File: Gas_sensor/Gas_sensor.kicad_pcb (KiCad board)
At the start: 2 copper layers, 100 x 73.5 mm, 69 parts, among them J1 Fix, J2 Fix, J3 Conn_01x03, J4 Conn_01x03, J5 Conn_01x03, J6 Conn_01x03, P1 Prog, Q1 PMV65UN, SW1 SW_Push, SW2 SW_Push, SW3 SW_Push, SW4 SW_Power, U1 MAX7219, U10 TPS61032PWP, U2 SCA103T-D04, U3 7SEGMENT_CC, U4 7SEGMENT_CC, U5 7SEGMENT_CC, U6 7SEGMENT_CC, U7 PIC16F18323_SOIC, U8 7SEGMENT_CC, U9 7SEGMENT_CC

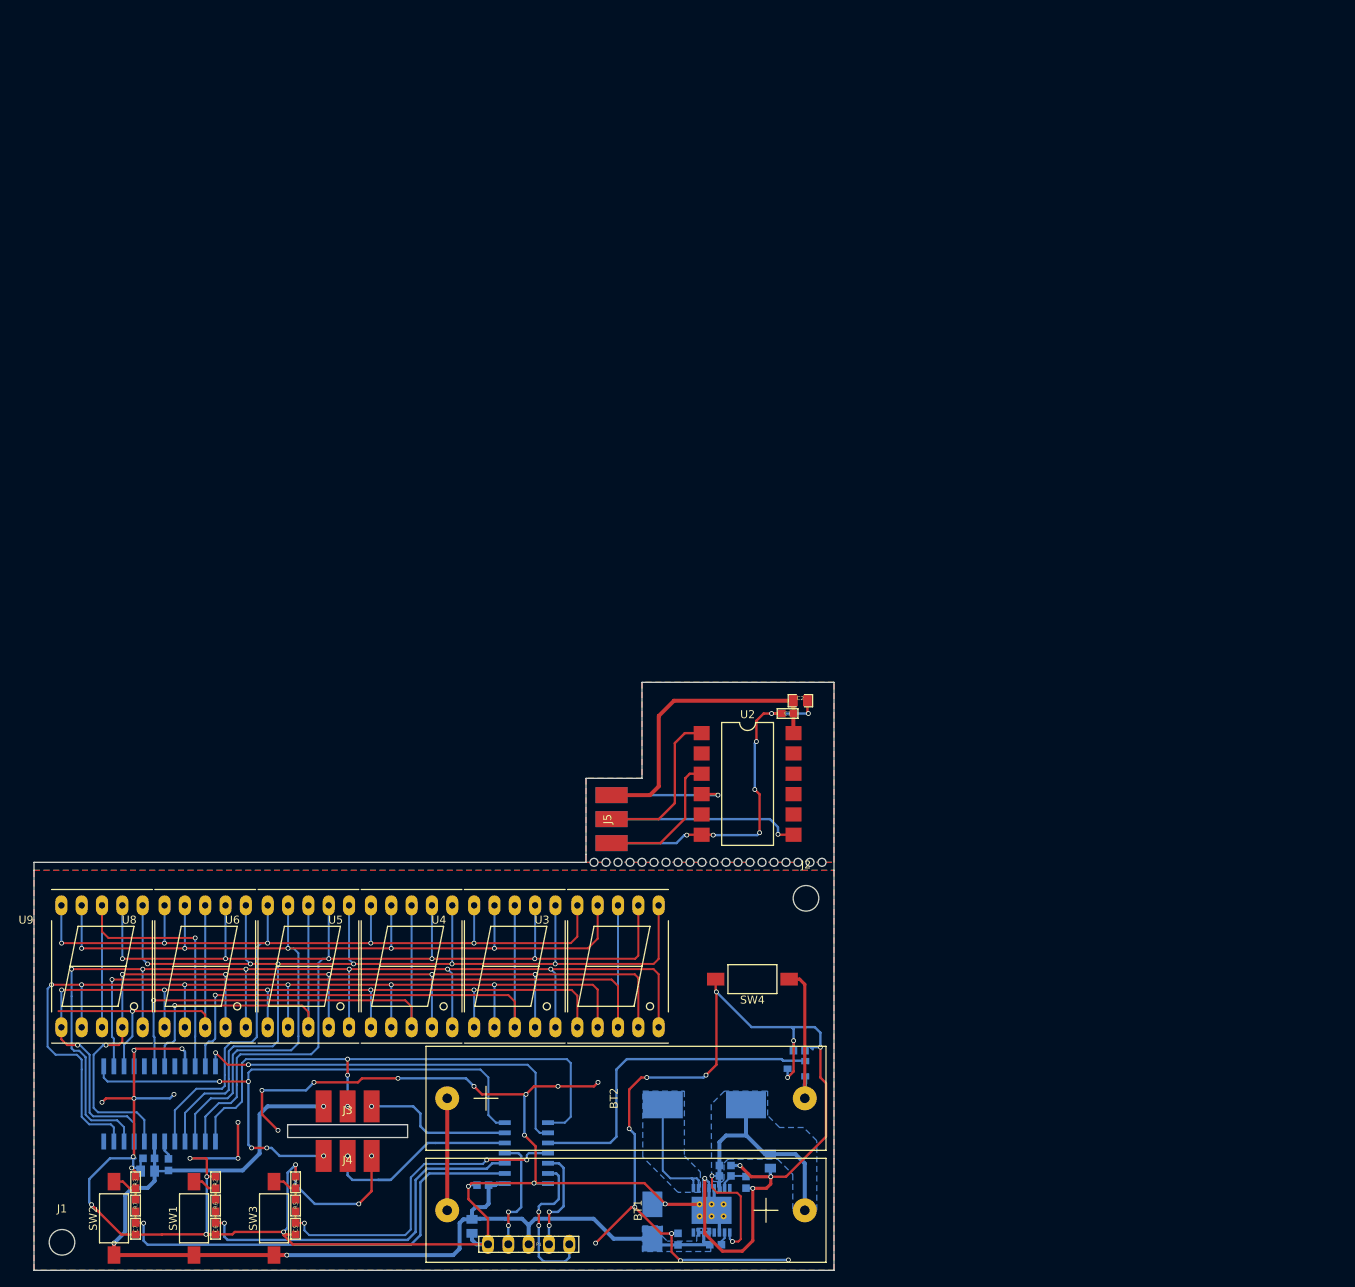
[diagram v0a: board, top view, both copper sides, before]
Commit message: update gas sensor schematic
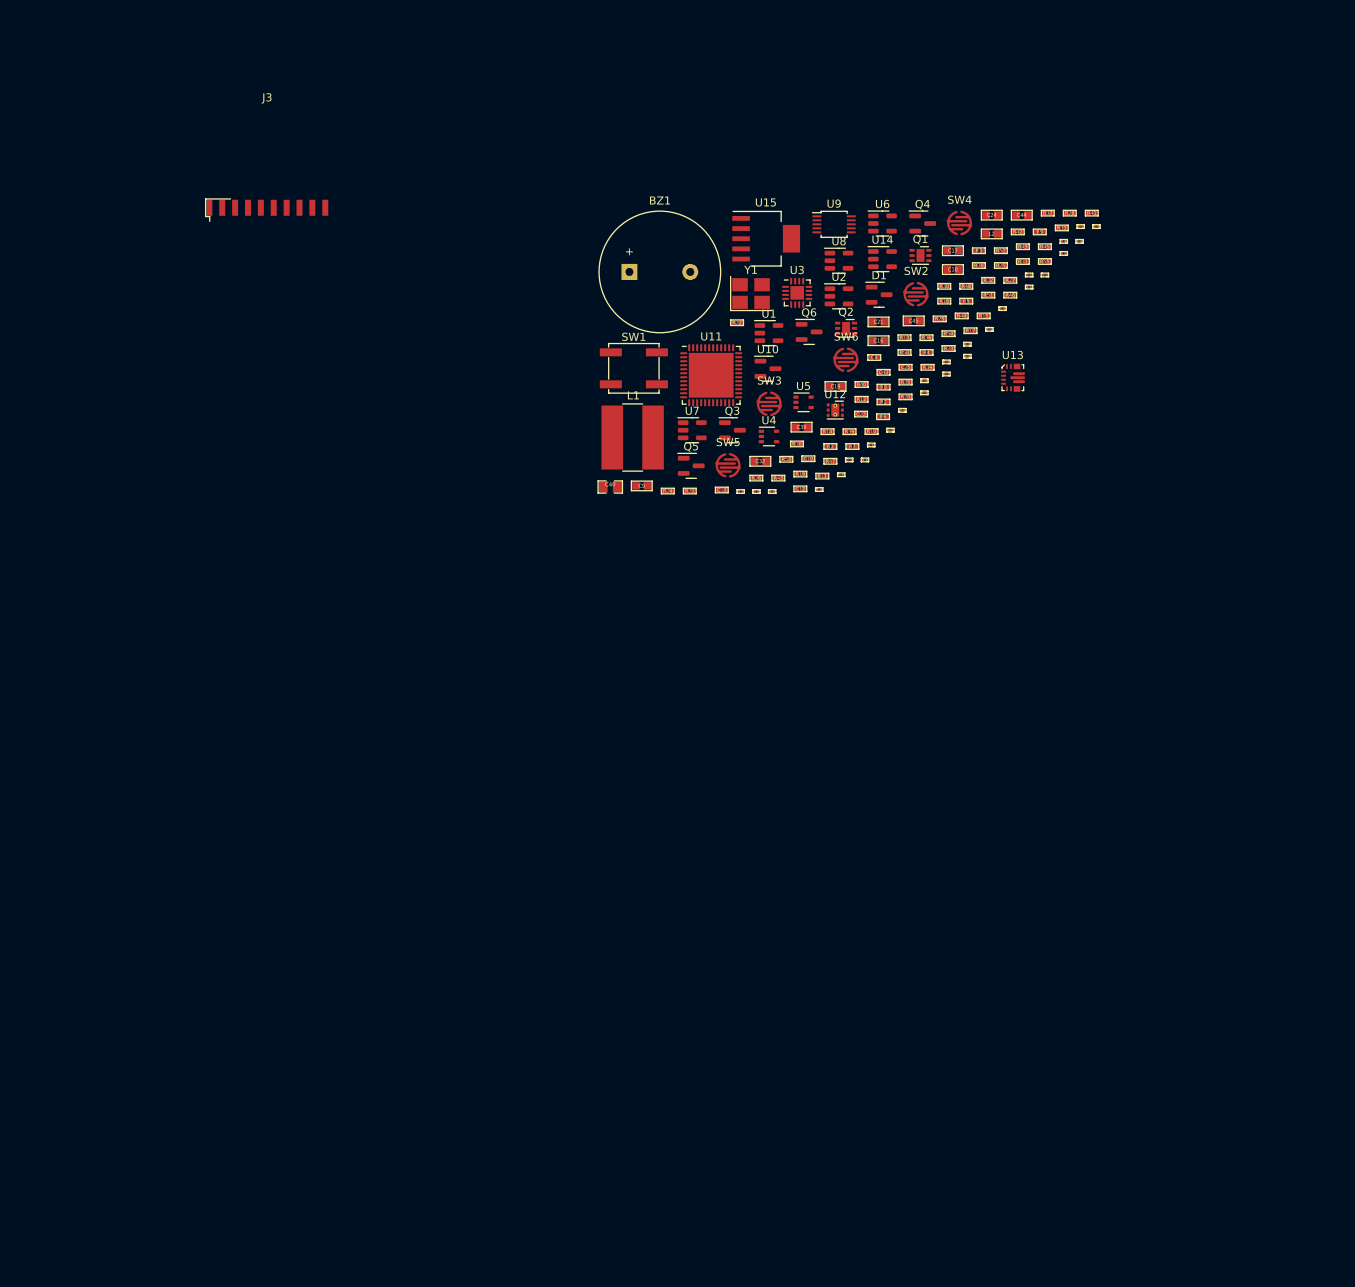
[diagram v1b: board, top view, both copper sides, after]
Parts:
- removed BT1, BT2: Keystone_2466, Yame_library:AAA_2466
- removed CutHole_1 (x20): VAL**, Yame_library:CutHole_1
- removed J1, J2: Fix, Mounting_Holes:MountingHole_3.2mm_M3
- removed J4, J5, J6: Conn_01x03, Yame_library:Inc_90°
- removed P1: Prog, Yame_library:HE10_14-5C-2.54-MR
- added BZ1: BUZZER, Buzzer_Beeper:Buzzer_15x7.5RM7.6, F.Cu at (99.4, 55.2)
- added C14: 100n, Yame_library:SM0201-MR, F.Cu at (155.7, 51.4)
- added C15: 100n, Yame_library:SM0201-MR, F.Cu at (146.1, 59.8)
- added C16: 1u, Yame_library:SM0603-MR, F.Cu at (130.6, 63.8)
- added C17: 1u, Yame_library:SM0603-MR, F.Cu at (139.9, 52.5)
- added C18: 1u, Yame_library:SM0603-MR, F.Cu at (139.9, 54.9)
- added C19: 1u, Yame_library:SM0603-MR, F.Cu at (125.2, 69.5)
- added C20: 100n, Yame_library:SM0201-MR, F.Cu at (133.6, 72.5)
- added C21: 2.2u, Yame_library:SM0603-MR, F.Cu at (130.6, 61.5)
- added C22: 100n, Yame_library:SM0201-MR, F.Cu at (141.7, 65.7)
- added C23: 8p, Yame_library:SM0402-MR, F.Cu at (128.4, 73.0)
- added C24: 1u, Yame_library:SM0603-MR, F.Cu at (144.7, 48.1)
- added C25: 8p, Yame_library:SM0402-MR, F.Cu at (133.9, 67.1)
- added C26: 100n, Yame_library:SM0201-MR, F.Cu at (149.4, 57.1)
- added C27: 100n, Yame_library:SM0201-MR, F.Cu at (157.8, 49.5)
- added C28: 100n, Yame_library:SM0201-MR, F.Cu at (132.1, 75.0)
- added C29: 100n, Yame_library:SM0201-MR, F.Cu at (141.7, 64.2)
- added C30: 100n, Yame_library:SM0201-MR, F.Cu at (136.3, 70.3)
- added C31: 100n, Yame_library:SM0201-MR, F.Cu at (144.4, 62.4)
- added C32: 22u, Yame_library:SM0603-MR, F.Cu at (115.8, 78.9)
- added C33: 100n, Yame_library:SM0201-MR, F.Cu at (128.9, 78.7)
- added C34: 100n, Yame_library:SM0201-MR, F.Cu at (139.1, 66.5)
- added C35: 100n, Yame_library:SM0201-MR, F.Cu at (129.7, 76.8)
- added C36: 100n, Yame_library:SM0201-MR, F.Cu at (136.3, 68.8)
- added C37: 100n, Yame_library:SM0201-MR, F.Cu at (139.1, 68.0)
- added C38: 100n, Yame_library:SM0201-MR, F.Cu at (153.7, 51.4)
- added C39: 10u, Yame_library:SM0603-MR, F.Cu at (120.9, 74.6)
- added C40: 47u, Yame_library:SM0805-MR, F.Cu at (97.0, 82.1)
- added C41: 100n, Yame_library:SM0201-MR, F.Cu at (155.8, 49.5)
- added C42: 100n, Yame_library:SM0201-MR, F.Cu at (117.3, 82.7)
- added C43: 10n, Yame_library:SM0402-MR, F.Cu at (131.2, 67.8)
- added C44: 10u, Yame_library:SM0603-MR, F.Cu at (148.5, 48.1)
- added C45: 10u, Yame_library:SM0603-MR, F.Cu at (135.0, 61.3)
- added D1: BAT54C, Package_TO_SOT_SMD:SOT-23, F.Cu at (130.6, 58.0)
- added L2: L_Ferrite, Yame_library:SM0603-MR, F.Cu at (144.7, 50.5)
- added Q2: DMC1229UFDB, Package_DFN_QFN:DFN-6-1EP_2x2mm_P0.65mm_EP1x1.6mm, F.Cu at (126.5, 62.2)
- added Q3: Q_NMOS_GSD, Package_TO_SOT_SMD:SOT-23, F.Cu at (112.3, 75.0)
- added Q4: Q_NMOS_GSD, Package_TO_SOT_SMD:SOT-23, F.Cu at (136.1, 49.1)
- added Q5: Q_NMOS_GSD, Package_TO_SOT_SMD:SOT-23, F.Cu at (107.2, 79.4)
- added Q6: Q_NMOS_GSD, Package_TO_SOT_SMD:SOT-23, F.Cu at (121.9, 62.7)
- added R13: 100, Yame_library:SM0402-MR, F.Cu at (133.8, 63.4)
- added R14: 22k, Yame_library:SM0402-MR, F.Cu at (124.2, 75.2)
- added R15: 22k, Yame_library:SM0402-MR, F.Cu at (143.7, 60.7)
- added R16: 22k, Yame_library:SM0402-MR, F.Cu at (120.4, 76.7)
- added R17: 2.2k, Yame_library:SM0402-MR, F.Cu at (142.1, 62.5)
- added R18: 2.2k, Yame_library:SM0402-MR, F.Cu at (138.8, 58.9)
- added R19: 2.2k, Yame_library:SM0402-MR, F.Cu at (120.8, 80.5)
- added R20: 2.2k, Yame_library:SM0402-MR, F.Cu at (133.9, 70.8)
- added R21: 0, Yame_library:SM0402-MR, F.Cu at (107.0, 82.6)
- added R22: 0, Yame_library:SM0402-MR, F.Cu at (112.9, 61.5)
- added R23: 0, Yame_library:SM0402-MR, F.Cu at (139.3, 64.8)
- added R24: 100k, Yame_library:SM0402-MR, F.Cu at (104.2, 82.6)
- added R25: 10k, Yame_library:SM0402-MR, F.Cu at (145.9, 54.4)
- added R26: 0, Yame_library:SM0402-MR, F.Cu at (115.3, 81.0)
- added R27: 0, Yame_library:SM0402-MR, F.Cu at (147.0, 56.2)
- added R28: 0, Yame_library:SM0402-MR, F.Cu at (154.5, 47.9)
- added R29: 390k, Yame_library:SM0402-MR, F.Cu at (138.2, 61.1)
- added R30: 390k, Yame_library:SM0402-MR, F.Cu at (138.8, 57.0)
- added R31: 390k, Yame_library:SM0402-MR, F.Cu at (148.6, 53.9)
- added R32: 390k, Yame_library:SM0402-MR, F.Cu at (144.3, 56.2)
- added R33: 390k, Yame_library:SM0402-MR, F.Cu at (153.5, 49.7)
- added R34: 390k, Yame_library:SM0402-MR, F.Cu at (136.7, 67.1)
- added R35: 390k, Yame_library:SM0402-MR, F.Cu at (133.9, 69.0)
- added R36: 390k, Yame_library:SM0402-MR, F.Cu at (136.6, 63.4)
- added R37: 10k, Yame_library:SM0402-MR, F.Cu at (151.7, 47.9)
- added R38: 100k, Yame_library:SM0402-MR, F.Cu at (143.1, 54.4)
- added R39: 100k, Yame_library:SM0402-MR, F.Cu at (126.9, 75.2)
- added R40: 22k, Yame_library:SM0402-MR, F.Cu at (128.4, 69.3)
- added R41: 22k, Yame_library:SM0402-MR, F.Cu at (157.2, 47.9)
- added R42: 22k, Yame_library:SM0402-MR, F.Cu at (148.0, 50.2)
- added R43: 3.9k, Yame_library:SM0402-MR, F.Cu at (118.0, 81.0)
- added R44: 3.9k, Yame_library:SM0402-MR, F.Cu at (141.0, 60.7)
- added R45: 100k, Yame_library:SM0402-MR, F.Cu at (151.4, 52.0)
- added R46: 100k, Yame_library:SM0402-MR, F.Cu at (147.0, 58.1)
- added R47: 100k, Yame_library:SM0402-MR, F.Cu at (124.5, 78.9)
- added R48: R, Yame_library:SM0402-MR, F.Cu at (141.5, 57.0)
- added R49: 910k, Yame_library:SM0402-MR, F.Cu at (148.6, 52.0)
- added R50: 43k, Yame_library:SM0402-MR, F.Cu at (133.8, 65.3)
- added R51: 100k, Yame_library:SM0402-MR, F.Cu at (144.3, 58.1)
- added R52: 3.9k, Yame_library:SM0402-MR, F.Cu at (145.9, 52.5)
- added R53: 3.9k, Yame_library:SM0402-MR, F.Cu at (119.0, 78.6)
- added R54: 3.9k, Yame_library:SM0402-MR, F.Cu at (139.3, 62.9)
- added R55: 100k, Yame_library:SM0402-MR, F.Cu at (151.4, 53.9)
- added R8: R, Yame_library:SM0402-MR, F.Cu at (131.2, 69.6)
- added SW5: SW_MEC_5G, Yame_library:SW_CARBON, F.Cu at (111.8, 79.4)
- added SW6: SW_MEC_5G, Yame_library:SW_CARBON, F.Cu at (126.5, 66.2)
- added U11: STM32F401CCUx, Package_DFN_QFN:QFN-48-1EP_7x7mm_P0.5mm_EP5.6x5.6mm, F.Cu at (109.7, 68.1)
- added U12: TMP117, Package_SON:WSON-6-1EP_2x2mm_P0.65mm_EP1x1.6mm_ThermalVias, F.Cu at (125.2, 72.5)
- added U13: TPS63070, Yame_library:VQFN-HR-15-1EP_3x2.5mm_P0.5m, F.Cu at (147.3, 68.4)
- added U14: TPS79333-EP, Package_TO_SOT_SMD:SOT-23-5, F.Cu at (131.1, 53.6)
- added U15: REG102GA, Package_TO_SOT_SMD:SOT-223-6, F.Cu at (116.5, 51.0)
- added Y1: 25MHz, Oscillator:Oscillator_SMD_Abracon_ASE-4Pin_3.2x2.5mm_HandSoldering, F.Cu at (114.6, 57.9)
- C1, C5, C6, C7: footprint Yame_library:SM0603-MR -> Yame_library:SM0201-MR
- C10: value 6TPE120MAZB -> 10n; footprint Capacitors_Tantalum_SMD:CP_Tantalum_Case-B_EIA-3528-21_Hand -> Yame_library:SM0402-MR; moved to F.Cu
- C11: value 2.2u -> 100n; footprint Yame_library:SM0603-MR -> Yame_library:SM0201-MR; moved to F.Cu
- C12: value 100n -> 100p; footprint Yame_library:SM0603-MR -> Yame_library:SM0402-MR; moved to F.Cu
- C13: value 10u -> 100p; footprint Yame_library:SM0805-MR -> Yame_library:SM0402-MR; moved to F.Cu
- C2: value 10u -> 100n; footprint Yame_library:SM0805-MR -> Yame_library:SM0201-MR
- C3, C8: footprint Yame_library:SM0603-MR -> Yame_library:SM0201-MR; moved to F.Cu
- C4: value 10u -> 10n; footprint Yame_library:SM0805-MR -> Yame_library:SM0402-MR; moved to F.Cu
- C9: footprint Yame_library:SM0805-MR -> Yame_library:SM0603-MR; moved to F.Cu
- J3: value Conn_01x03 -> Conn_01x10; footprint Yame_library:Inc_90° -> Yame_library:LCD_Contact_1x10_P2.54mm
- L1: value MLC1565-472MLB -> 1.5uH; footprint Yame_library:MLC15xx -> Yame_library:L_Bourns-SDR0805_7.8x8mm; moved to F.Cu
- Q1: value PMV65UN -> DMC1229UFDB; footprint Yame_library:SOT23-MR -> Package_DFN_QFN:DFN-6-1EP_2x2mm_P0.65mm_EP1x1.6mm; moved to F.Cu
- R1: value 33k -> 0; footprint Yame_library:SM0603-MR -> Yame_library:SM0402-MR; moved to F.Cu
- R10: value 1.02M -> R; footprint Yame_library:SM0603-MR -> Yame_library:SM0402-MR; moved to F.Cu
- R11: value 390k -> 100; footprint Yame_library:SM0603-MR -> Yame_library:SM0402-MR; moved to F.Cu
- R12: value 1M -> 100; footprint Yame_library:SM0603-MR -> Yame_library:SM0402-MR; moved to F.Cu
- R2: value 10k -> 0; footprint Yame_library:SM0603-MR -> Yame_library:SM0402-MR
- R3, R4: value 10k -> R; footprint Yame_library:SM0603-MR -> Yame_library:SM0402-MR
- R5, R6: value 100k -> R; footprint Yame_library:SM0603-MR -> Yame_library:SM0402-MR
- R7: value 100k -> 0; footprint Yame_library:SM0603-MR -> Yame_library:SM0402-MR
- R9: value 1.02M -> 0; footprint Yame_library:SM0603-MR -> Yame_library:SM0402-MR; moved to F.Cu
- SW1: value SW_Push -> SW_MEC_5G; footprint Buttons_Switches_SMD:SW_SPST_FSMSM -> Button_Switch_SMD:SW_SPST_EVPBF
- SW2, SW3: value SW_Push -> SW_MEC_5G; footprint Buttons_Switches_SMD:SW_SPST_FSMSM -> Yame_library:SW_CARBON
- SW4: value SW_Power -> SW_MEC_5G; footprint Buttons_Switches_SMD:SW_SPST_FSMSM -> Yame_library:SW_CARBON
- U1: value MAX7219 -> LPV511; footprint Housings_SOIC:SOIC-24W_7.5x15.4mm_Pitch1.27mm -> Package_TO_SOT_SMD:SOT-23-5; moved to F.Cu
- U10: value TPS61032PWP -> MCP1700-3302E_SOT23; footprint Housings_SSOP:HTSSOP-16-1EP_4.4x5mm_Pitch0.65mm_ThermalVias -> Package_TO_SOT_SMD:SOT-23; moved to F.Cu
- U2: value SCA103T-D04 -> LPV511; footprint Housings_DIP:SMDIP-12_W11.48mm -> Package_TO_SOT_SMD:SOT-23-5
- U3: value 7SEGMENT_CC -> MCP47CMB22; footprint Displays_7-Segment:7SegmentLED_LTS6760_LTS6780 -> Package_DFN_QFN:QFN-16-1EP_3x3mm_P0.5mm_EP1.7x1.7mm
- U4: value 7SEGMENT_CC -> MCP6V71; footprint Displays_7-Segment:7SegmentLED_LTS6760_LTS6780 -> Package_TO_SOT_SMD:SOT-353_SC-70-5
- U5: value 7SEGMENT_CC -> LPV511; footprint Displays_7-Segment:7SegmentLED_LTS6760_LTS6780 -> Package_TO_SOT_SMD:SOT-353_SC-70-5
- U6, U8: value 7SEGMENT_CC -> MCP6V71; footprint Displays_7-Segment:7SegmentLED_LTS6760_LTS6780 -> Package_TO_SOT_SMD:SOT-23-5
- U7: value PIC16F18323_SOIC -> MCP6V71; footprint Housings_SOIC:SOIC-14_3.9x8.7mm_Pitch1.27mm -> Package_TO_SOT_SMD:SOT-23-5; moved to F.Cu
- U9: value 7SEGMENT_CC -> ADS1115IDGS; footprint Displays_7-Segment:7SegmentLED_LTS6760_LTS6780 -> Package_SO:TSSOP-10_3x3mm_P0.5mm
- moved R3 157.1 mm to (143.1, 52.5), turned to 0 degrees
- moved C6 156.7 mm to (149.4, 55.6), turned to 0 degrees
- moved C5 155.2 mm to (153.7, 52.9), turned to 0 degrees
- moved SW2 152.9 mm to (135.2, 58.0), turned to 0 degrees
- moved R5 140.7 mm to (141.5, 58.9), turned to 0 degrees
- moved C4 136.4 mm to (130.0, 65.9), turned to 0 degrees
- moved R9 132.9 mm to (150.7, 50.2)
- moved R7 130.5 mm to (127.3, 77.0), turned to 0 degrees
- moved R4 130.3 mm to (136.6, 65.3), turned to 0 degrees
- moved U9 130.3 mm to (125.0, 49.2)
- moved R6 129.2 mm to (131.1, 73.3), turned to 0 degrees
- moved R2 128.4 mm to (131.2, 71.5), turned to 0 degrees
- moved U1 122.8 mm to (116.9, 62.9), turned to 0 degrees
- moved R1 122.1 mm to (124.5, 77.0), turned to 0 degrees
- moved SW1 119.6 mm to (100.0, 67.2), turned to 0 degrees
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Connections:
- C1 pad 1: /+5v_R -> +3V3
- C1 pad 2: /GND_R -> GND
- C10 pad 1: /+5v -> +9V
- C11 pad 1: /+5v -> +9V
- C12 pad 1: /+Vbat -> /Iheater
- C13 pad 1: /+Vbat -> /Isensor
- C2 pad 1: /+5v_R -> +3V3
- C2 pad 2: /GND_R -> GND
- C3 pad 1: /+5v -> +3V3
- C4 pad 1: /+5v -> +3V3
- C5 pad 1: Net-(C5-Pad1) -> +3V3
- C6 pad 1: Net-(C6-Pad1) -> +9V
- C7 pad 1: Net-(C7-Pad1) -> +3V3
- C8 pad 1: /+5v -> +9V
- C9 pad 1: /+5v -> +3V3
- J3 pad 1: /+5v -> /Vcomm0
- J3 pad 2: /SCK -> /Vcomm1
- J3 pad 3: /MISO -> /Vcomm2
- L1 pad 1: /+Vbat -> Net-(L1-Pad1)
- L1 pad 2: /+Vsw -> Net-(L1-Pad2)
- Q1 pad 1: /Von -> Net-(Q1-Pad1)
- Q1 pad 2: /BATT_LowSide -> Net-(Q1-Pad2)
- Q1 pad 3: GND -> Net-(J1-Pad2)
- R1 pad 1: /+5v -> Net-(R1-Pad1)
- R1 pad 2: Net-(R1-Pad2) -> GND
- R10 pad 1: /+Vbat -> +9V
- R10 pad 2: Net-(R10-Pad2) -> Net-(Q2-Pad4)
- R11 pad 1: Net-(R10-Pad2) -> /Vsensor
- R11 pad 2: GND -> /ADC0
- R12 pad 1: /Von -> /Vheater
- R12 pad 2: GND -> /ADC1
- R3 pad 1: Net-(R3-Pad1) -> +3V3
- R3 pad 2: GND -> Net-(Q1-Pad6)
- R4 pad 1: Net-(R4-Pad1) -> Net-(Q1-Pad2)
- R5 pad 1: Net-(C5-Pad1) -> +9V
- R5 pad 2: Net-(R4-Pad1) -> Net-(Q2-Pad6)
- R6 pad 1: Net-(C6-Pad1) -> Net-(Q2-Pad2)
- R6 pad 2: Net-(R2-Pad1) -> GND
- R7 pad 1: Net-(C7-Pad1) -> Net-(R7-Pad1)
- R7 pad 2: Net-(R3-Pad1) -> /Iheater
- R9 pad 1: /+5v -> Net-(R9-Pad1)
- R9 pad 2: Net-(R9-Pad2) -> /Isensor
- SW1 pad 1: /+5v -> Net-(R38-Pad2)
- SW1 pad 2: Net-(R2-Pad1) -> Net-(R38-Pad2)
- SW2 pad 1: /+5v -> Net-(R39-Pad2)
- SW2 pad 2: Net-(R3-Pad1) -> Net-(R39-Pad2)
- SW3 pad 1: /+5v -> Net-(R45-Pad2)
- SW3 pad 2: Net-(R4-Pad1) -> Net-(R45-Pad2)
- SW4 pad 1: /BATT_LowSide -> Net-(R46-Pad2)
- SW4 pad 2: GND -> Net-(R46-Pad2)
- U1 pad 1: /MOSI -> /Vref_DAC
- U1 pad 2: /D0 -> GND
- U1 pad 3: /D4 -> Net-(U1-Pad3)
- U1 pad 4: GND -> /Vref_DAC
- U1 pad 5: Net-(U1-Pad5) -> +3V3
- U10 pad 1: /+Vsw -> GND
- U10 pad 2: /+Vsw -> +3V3
- U10 pad 3: GND -> +BATT
- U2 pad 1: /SCK_R -> Net-(Q1-Pad1)
- U2 pad 2: Net-(U2-Pad2) -> GND
- U2 pad 3: /MISO_R -> /Isensor
- U2 pad 4: /MOSI_R -> Net-(Q1-Pad2)
- U2 pad 5: Net-(U2-Pad5) -> +3V3
- U3 pad 1: /E -> Net-(R2-Pad1)
- U3 pad 10: /G -> GND
- U3 pad 2: /D -> Net-(U1-Pad3)
- U3 pad 3: /D0 -> Net-(R9-Pad1)
- U3 pad 4: /C -> unconnected-(U3-Pad4)
- U3 pad 5: /DP -> Net-(R7-Pad1)
- U3 pad 6: /B -> (no net)
- U3 pad 7: /A -> (no net)
- U3 pad 8: /D0 -> unconnected-(U3-Pad8)
- U3 pad 9: /F -> unconnected-(U3-Pad9)
- U4 pad 1: /E -> Net-(Q2-Pad1)
- U4 pad 2: /D -> GND
- U4 pad 3: /D1 -> /Iheater
- U4 pad 4: /C -> Net-(Q2-Pad2)
- U4 pad 5: /DP -> +9V
- U5 pad 1: /E -> Net-(Q1-Pad5)
- U5 pad 2: /D -> GND
- U5 pad 3: /D2 -> Net-(Q1-Pad6)
- U5 pad 4: /C -> Net-(Q1-Pad4)
- U5 pad 5: /DP -> +3V3
- U6 pad 1: /E -> Net-(Q2-Pad5)
- U6 pad 2: /D -> +9V
- U6 pad 3: /D3 -> Net-(Q2-Pad4)
- U6 pad 4: /C -> Net-(Q2-Pad6)
- U6 pad 5: /DP -> GND
- U7 pad 1: /+5v -> /Vsensor
- U7 pad 2: Net-(C7-Pad1) -> GND
- U7 pad 3: Net-(C6-Pad1) -> Net-(J1-Pad2)
- U7 pad 4: Net-(P1-Pad4) -> /Vsensor
- U7 pad 5: //CS_INC -> +3V3
- U8 pad 1: /E -> Net-(R14-Pad1)
- U8 pad 2: /D -> GND
- U8 pad 3: /D4 -> Net-(J1-Pad3)
- U8 pad 4: /C -> Net-(R14-Pad1)
- U8 pad 5: /DP -> +9V
- U9 pad 1: /E -> +3V3
- U9 pad 10: /G -> /SCL
- U9 pad 2: /D -> /~{RDY}
- U9 pad 3: /D5 -> GND
- U9 pad 4: /C -> Net-(R21-Pad2)
- U9 pad 5: /DP -> Net-(R22-Pad2)
- U9 pad 6: /B -> Net-(R23-Pad2)
- U9 pad 7: /A -> unconnected-(U9-Pad7)
- U9 pad 8: /D5 -> +3V3
- U9 pad 9: /F -> /SDA
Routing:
- net GND: track 427.2 -> 0.00 mm, vias 45 -> 0
- net /DP: track 143.7 -> 0.00 mm, vias 6 -> 0
- net /A: track 140.1 -> 0.00 mm, vias 5 -> 0
- net /B: track 139.6 -> 0.00 mm, vias 6 -> 0
- net /+5v: track 138.7 -> 0.00 mm, vias 3 -> 0
- net /F: track 131.7 -> 0.00 mm, vias 5 -> 0
- net /C: track 126.4 -> 0.00 mm, vias 6 -> 0
- net /D: track 126.2 -> 0.00 mm, vias 6 -> 0
- net /G: track 125.8 -> 0.00 mm, vias 5 -> 0
- net /E: track 113.6 -> 0.00 mm, vias 6 -> 0
- net /D0: track 94.9 -> 0.00 mm, vias 1 -> 0
- net /MOSI: track 76.4 -> 0.00 mm, vias 5 -> 0
- net /SCK: track 69.3 -> 0.00 mm, vias 3 -> 0
- net /D1: track 65.9 -> 0.00 mm, vias 1 -> 0
- net /D2: track 58.7 -> 0.00 mm, vias 1 -> 0
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- removed copper zone on B.Cu, net /+5v
- removed copper zone on B.Cu, net /+Vbat
- removed copper zone on B.Cu, net /+Vsw
- removed copper zone on B.Cu, net /GND_R
- removed copper zone on F.Cu, net /GND_R
- removed copper zone on B.Cu, net GND
- removed copper zone on F.Cu, net GND
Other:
- board outline removed
- net class Default removed

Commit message: update sch, start layout
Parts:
- added J1: Conn_02x02_Counter_Clockwise, Connector_PinHeader_2.54mm:PinHeader_1x04_P2.54mm_Vertical, F.Cu at (140.3, 34.7)
- added J2: Conn_01x04, Connector_PinHeader_2.54mm:PinHeader_1x04_P2.54mm_Vertical, F.Cu at (129.4, 87.2)
- added J4: Conn_01x01, Yame_library:Conn1_batt, F.Cu at (145.1, 34.8)
- added J5: Conn_01x01, Yame_library:Conn1_batt, F.Cu at (150.0, 34.8)
- added SW10: SW_Push, Button_Switch_SMD:SW_SPST_EVPBF, F.Cu at (179.0, 99.9)
- added SW11: SW_Push, Yame_library:SW_CARBON, F.Cu at (156.0, 105.9)
- added SW12: SW_Push, Yame_library:SW_CARBON, F.Cu at (173.3, 105.9)
- added SW7: SW_Push, Button_Switch_SMD:SW_SPST_EVPBF, F.Cu at (168.9, 92.4)
- added SW8: SW_Push, Yame_library:SW_CARBON, F.Cu at (169.0, 105.9)
- added SW9: SW_Push, Button_Switch_SMD:SW_SPST_EVPBF, F.Cu at (168.9, 99.9)
- Q1, Q2: footprint Package_DFN_QFN:DFN-6-1EP_2x2mm_P0.65mm_EP1x1.6mm -> Yame_library:U-DFN2020-6_2x2mm_P0.65mm_EP0.6mm
- SW1, SW3, SW4, SW6: value SW_MEC_5G -> SW_Push
- SW2, SW5: value SW_MEC_5G -> SW_Push; footprint Yame_library:SW_CARBON -> Button_Switch_SMD:SW_SPST_EVPBF
- moved SW5 68.5 mm to (179.0, 92.4)
- moved SW1 67.4 mm to (158.9, 99.9)
- moved SW4 61.7 mm to (186.2, 90.8)
- moved SW3 55.3 mm to (160.3, 105.9)
- moved SW6 55.1 mm to (164.7, 105.9)
- moved U13 47.7 mm to (118.2, 106.2)
- moved SW2 41.7 mm to (158.9, 92.4)
- moved L1 30.0 mm to (109.7, 104.3)
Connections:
- SW1 pad 2: Net-(R38-Pad2) -> GND
- SW2 pad 2: Net-(R39-Pad2) -> GND
- SW3 pad 1: Net-(R45-Pad2) -> Net-(R38-Pad2)
- SW3 pad 2: Net-(R45-Pad2) -> GND
- SW4 pad 1: Net-(R46-Pad2) -> Net-(R39-Pad2)
- SW4 pad 2: Net-(R46-Pad2) -> GND
- SW5 pad 1: Net-(R47-Pad2) -> Net-(R45-Pad2)
- SW5 pad 2: Net-(R47-Pad2) -> GND
- SW6 pad 2: Net-(J5-Pad1) -> GND
